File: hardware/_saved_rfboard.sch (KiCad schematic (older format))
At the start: 20 parts, among them J1 10118194-0001LF, J2 Conn_01x10, J3 Conn_01x10, P2 CONN_01X03, P3 CONN_01X04, P5 CONN_01X01, U1 SAMD21E18, U2 RFM69CW-915MHZ, U3 MIC5504-3.3YM5-T5, U4 74LVC1G125

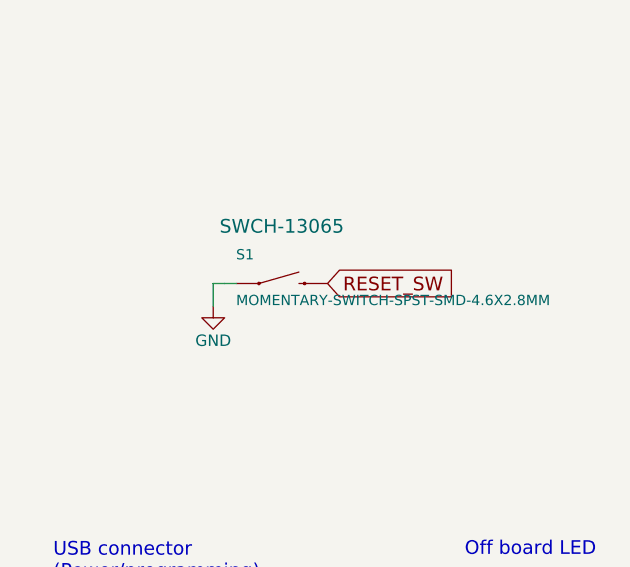
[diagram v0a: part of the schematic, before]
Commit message: Hardware revision 1.1:
- Add a buffer to bump up the signal to the serial LED to 5V
- Switch SWD progamming input voltage to 5V
- Add a reset button
- Remove two less-useful pins
- Make the board two breadboard rows smaller
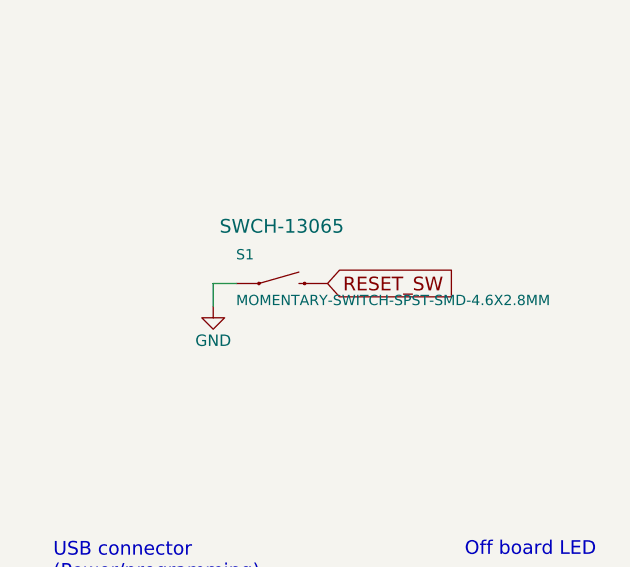
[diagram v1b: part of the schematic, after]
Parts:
- U2: footprint homebrew:RFM69CW -> homebrew:RFM69CW-minimalpads
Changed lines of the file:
@@
 F 0 "U2" H 4500 2250 45  0000 L BNN
 F 1 "RFM69CW-915MHZ" H 4500 1100 45  0000 L BNN
-F 2 "homebrew:RFM69CW" H 4900 2300 20  0001 C CNN
+F 2 "homebrew:RFM69CW-minimalpads" H 4900 2300 20  0001 C CNN
 F 3 "" H 4900 1700 60  0001 C CNN
 F 4 "IC-11996" H 4900 2350 60  0000 C CNN "Field4"
@@
 	1300 5550 1300 5450
 Wire Wire Line
-	1300 5450 1350 5450
-Wire Wire Line
-	1350 5450 1400 5450
+	1300 5450 1400 5450
 Text GLabel 1800 5450 2    60   Input ~ 0
 RESET_SW
